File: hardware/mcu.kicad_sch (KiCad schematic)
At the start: 32 parts, among them J301 USB_C_Receptacle_USB2.0, SW301 RESET, SW302 BOOTSEL, U301 USBLC6-2SC6, U302 ESP32-C3, Y301 40 MHz

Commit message: WIP pcb layout
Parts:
- removed L302: CMF3216F-900-2P-T, lzptr:CMC-1206, symbol Device:Filter_EMI_LL_1423
- J301: symbol Connector:USB_C_Receptacle_USB2.0_14P -> Connector:USB_C_Receptacle_USB2.0_16P
- SW302: value BOOTSEL -> BOOT
- renumbered L303 to L302
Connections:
- net USB_CMC_D+ is gone; now on net USB_D+: U301.4 (I/O2)
- net USB_CMC_D- is gone; now on net USB_D-: U301.6 (I/O1)
- net ACT: now also U302.16 (GPIO10); no longer U302.9 (MTMS/GPIO4/ADC1_CH4)
- net I2C_CLK: now also U302.8 (GPIO3/ADC1_CH3); no longer U302.5 (XTAL_32K_N/ADC1_CH1)
- net I2C_DATA: now also U302.9 (MTMS/GPIO4/ADC1_CH4); no longer U302.4 (XTAL_32K_P/ADC1_CH0)
- net LNA_IN: now reaches C304.1, L301.2, U302.1 (LNA_IN)
- net GP8: now reaches R305.2, U302.14 (GPIO8)
- net GP2: now reaches R304.2, U302.6 (GPIO2/ADC1_CH2)
- no-connect marks 14 -> 16
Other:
- note added: "Flash efuses to fixed 3.3V to use MTDI as normal pin https://docs.espressif.com/projects/esptool/en/latest/esp32c3/espefuse/set-flash-voltage-cmd.html"
- note added: "Signal Path: Connector <-> ESD Protection <-> MCU"
- note removed: "Common-Mode Choke Impedance: 90R"
- note removed: "Pull MTDI low or leave unconnected to use internal regulator for the in package Flash Leave VDD_SPI unconnected https://docs.espressif.com/projects/esptool/en/latest/esp32c3/espefuse/set-flash-voltage-cmd.html"
- note removed: "Signal Path: Connector <-> ESD Protection <-> Common-Mode Choke <-> MCU"

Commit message: Finished the pcb layout
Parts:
- AE301: footprint lzptr:ANT_16060A1T_WAL-L -> lzptr:ANT5320LL45R2400A; MPN C127620 -> C723371
- D301: MPN C72043 -> C12624
- J301: Position Offset (none) -> 0,1.45
- U302: value ESP32-C3 -> ESP32-C3FH4; MPN (none) -> C2858491; Rotation Offset (none) -> -90
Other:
- note added: "CL = 10pF"
- note removed: "CL = 9pF"
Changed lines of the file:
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@@
 		)
 	)
-	(text "CL = 9pF"
+	(text "CL = 10pF"
 		(exclude_from_sim no)
 		(at 63.246 75.692 0)
@@
 			)
 		)
-		(property "Value" "ESP32-C3"
+		(property "Value" "ESP32-C3FH4"
 			(at 153.3241 119.38 0)
 			(effects
@@
 			)
 		)
-		(property "MPN" ""
+		(property "MPN" "C2858491"
+			(at 151.13 86.36 0)
+			(effects
+				(font
+					(size 1.27 1.27)
+				)
+				(hide yes)
+			)
+		)
+		(property "Rotation Offset" "-90"
 			(at 151.13 86.36 0)
 			(effects
@@
 			)
 		)
-		(property "Footprint" "lzptr:ANT_16060A1T_WAL-L"
+		(property "Footprint" "lzptr:ANT5320LL45R2400A"
 			(at 58.42 49.53 0)
 			(effects
@@
 			)
 		)
-		(property "MPN" "C127620"
+		(property "MPN" "C723371"
 			(at 58.42 49.53 0)
 			(effects
@@
 			)
 		)
-		(property "MPN" "C72043"
+		(property "MPN" "C12624"
 			(at 267.97 135.89 0)
 			(effects
@@
 			)
 		)
+		(property "Position Offset" "0,1.45"
+			(at 43.18 162.56 0)
+			(effects
+				(font
+					(size 1.27 1.27)
+				)
+				(hide yes)
+			)
+		)

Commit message: release: v0.1
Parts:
- AE301: footprint lzptr:ANT5320LL45R2400A -> lzptr:Rainsun-AN9520-245; MPN C723371 -> C99665
- D301: footprint LED_SMD:LED_0603_1608Metric -> LED_SMD:LED_0805_2012Metric; MPN C12624 -> C2297
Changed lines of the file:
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@@
 	(title_block
 		(title "Radiator Booster")
-		(date "2024-11-17")
+		(date "2025-01-19")
 		(rev "0.1")
 		(company "LP")
@@
 			)
 		)
-		(property "Footprint" "lzptr:ANT5320LL45R2400A"
+		(property "Footprint" "lzptr:Rainsun-AN9520-245"
 			(at 58.42 49.53 0)
 			(effects
@@
 			)
 		)
-		(property "MPN" "C723371"
+		(property "MPN" "C99665"
 			(at 58.42 49.53 0)
 			(effects
@@
 			)
 		)
-		(property "Footprint" "LED_SMD:LED_0603_1608Metric"
+		(property "Footprint" "LED_SMD:LED_0805_2012Metric"
 			(at 267.97 135.89 0)
 			(effects
@@
 			)
 		)
-		(property "MPN" "C12624"
+		(property "MPN" "C2297"
 			(at 267.97 135.89 0)
 			(effects

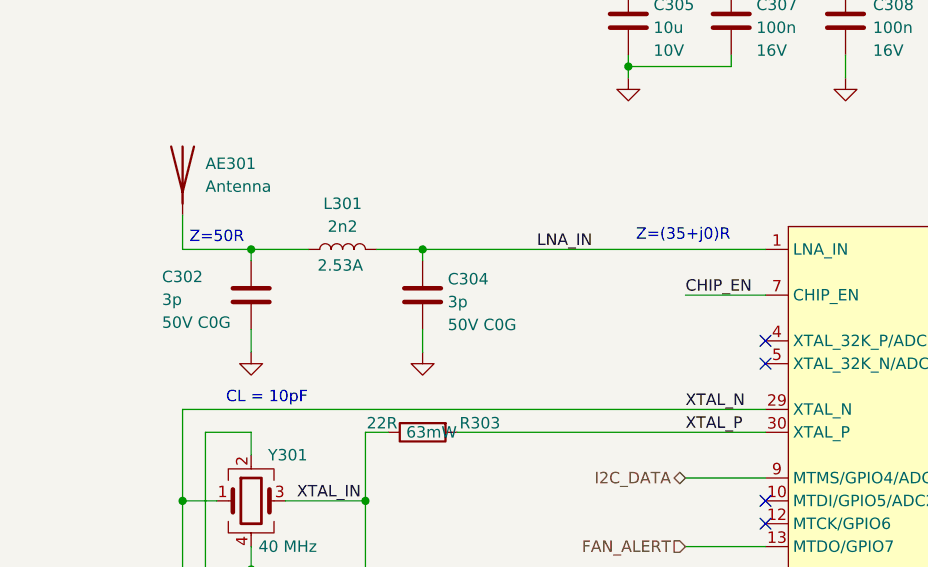
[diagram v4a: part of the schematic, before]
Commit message: Fixed routing at intel pwm fan connectors
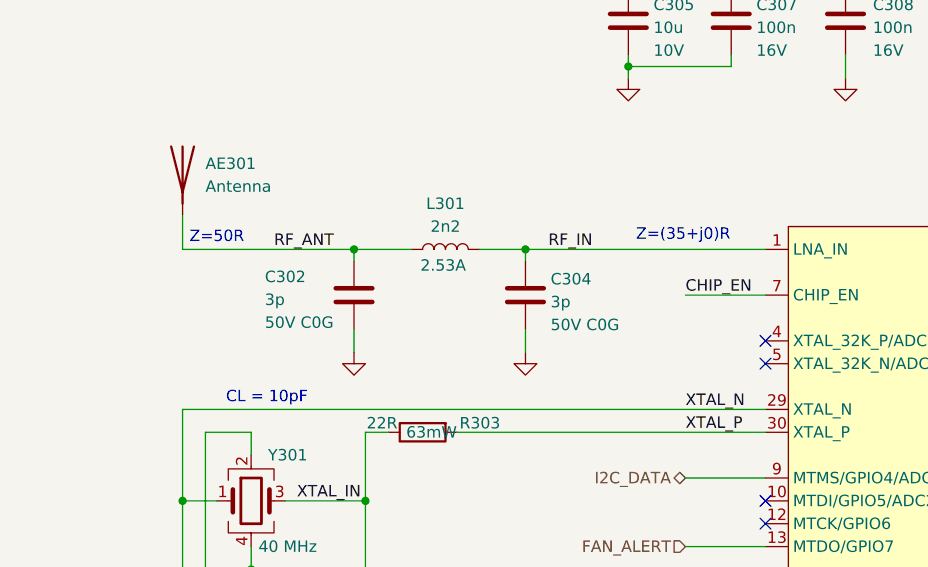
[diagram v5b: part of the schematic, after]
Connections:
- net RF_ANT: now reaches AE301.1 (A), C302.1, L301.1
- net LNA_IN renamed RF_IN
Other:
- moved on the sheet: C302, C304, L301
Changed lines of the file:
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@@
 	)
 	(junction
-		(at 85.09 58.42)
+		(at 96.52 58.42)
 		(diameter 0)
 		(color 0 0 0 0)
@@
 	)
 	(junction
-		(at 66.04 58.42)
+		(at 77.47 58.42)
 		(diameter 0)
 		(color 0 0 0 0)
@@
 	(wire
 		(pts
-			(xy 72.39 58.42) (xy 66.04 58.42)
+			(xy 83.82 58.42) (xy 77.47 58.42)
 		)
 		(stroke
@@
 	(wire
 		(pts
-			(xy 85.09 67.31) (xy 85.09 69.85)
+			(xy 96.52 67.31) (xy 96.52 69.85)
 		)
 		(stroke
@@
 	(wire
 		(pts
-			(xy 85.09 58.42) (xy 85.09 59.69)
+			(xy 96.52 58.42) (xy 96.52 59.69)
 		)
 		(stroke
@@
 	(wire
 		(pts
-			(xy 66.04 58.42) (xy 66.04 59.69)
+			(xy 77.47 58.42) (xy 77.47 59.69)
 		)
 		(stroke
@@
 	(wire
 		(pts
-			(xy 123.19 58.42) (xy 85.09 58.42)
-		)
-		(stroke
-			(width 0)
-			(type default)
-		)
-	)
-	(wire
-		(pts
 			(xy 78.74 160.02) (xy 63.5 160.02)
 		)
@@
 	(wire
 		(pts
-			(xy 80.01 58.42) (xy 85.09 58.42)
+			(xy 91.44 58.42) (xy 96.52 58.42)
 		)
 		(stroke
@@
 	(wire
 		(pts
-			(xy 58.42 58.42) (xy 66.04 58.42)
+			(xy 58.42 58.42) (xy 77.47 58.42)
 		)
 		(stroke
@@
 	(wire
 		(pts
+			(xy 96.52 58.42) (xy 123.19 58.42)
+		)
+		(stroke
+			(width 0)
+			(type default)
+		)
+	)
+	(wire
+		(pts
 			(xy 153.67 41.91) (xy 156.21 41.91)
 		)
@@
 	(wire
 		(pts
-			(xy 66.04 69.85) (xy 66.04 67.31)
+			(xy 77.47 69.85) (xy 77.47 67.31)
 		)
 		(stroke
@@
 		)
 	)
+	(label "RF_ANT"
+		(at 68.58 58.42 0)
+		(effects
+			(font
+				(size 1.27 1.27)
+			)
+			(justify left bottom)
+		)
+	)
 	(label "XTAL_N"
 		(at 114.3 76.2 0)
@@
 		)
 	)
-	(label "LNA_IN"
-		(at 97.79 58.42 0)
+	(label "RF_IN"
+		(at 99.06 58.42 0)
 		(effects
 			(font
@@
 	(symbol
 		(lib_id "power:GND")
-		(at 66.04 69.85 0)
+		(at 77.47 69.85 0)
 		(unit 1)
 		(exclude_from_sim no)
@@
 		(fields_autoplaced yes)
 		(property "Reference" "#PWR0303"
-			(at 66.04 76.2 0)
+			(at 77.47 76.2 0)
 			(effects
 				(font
@@
 		)
 		(property "Value" "GND"
-			(at 66.04 74.93 0)
+			(at 77.47 74.93 0)
 			(effects
 				(font
@@
 		)
 		(property "Footprint" ""
-			(at 66.04 69.85 0)
+			(at 77.47 69.85 0)
 			(effects
 				(font
@@
 		)
 		(property "Datasheet" ""
-			(at 66.04 69.85 0)
+			(at 77.47 69.85 0)
 			(effects
 				(font
@@
 		)
 		(property "Description" "Power symbol creates a global label with name \"GND\" , ground"
-			(at 66.04 69.85 0)
+			(at 77.47 69.85 0)
 			(effects
 				(font
@@
 		)
 		(property "Rating" ""
-			(at 66.04 69.85 0)
+			(at 77.47 69.85 0)
 			(effects
 				(font
@@
 		)
 		(property "MPN" ""
-			(at 66.04 69.85 0)
+			(at 77.47 69.85 0)
 			(effects
 				(font
@@
 	(symbol
 		(lib_id "Device:C")
-		(at 85.09 63.5 0)
+		(at 96.52 63.5 0)
 		(unit 1)
 		(exclude_from_sim no)
@@
 		(dnp no)
 		(property "Reference" "C304"
-			(at 87.884 61.722 0)
+			(at 99.314 61.722 0)
 			(effects
 				(font
@@
 		)
 		(property "Value" "3p"
-			(at 87.884 64.262 0)
+			(at 99.314 64.262 0)
 			(effects
 				(font
@@
 		)
 		(property "Footprint" "Capacitor_SMD:C_0402_1005Metric"
-			(at 86.0552 67.31 0)
+			(at 97.4852 67.31 0)
 			(effects
 				(font
@@
 		)
 		(property "Datasheet" "~"
-			(at 85.09 63.5 0)
+			(at 96.52 63.5 0)
 			(effects
 				(font
@@
 		)
 		(property "Description" "Unpolarized capacitor"
-			(at 85.09 63.5 0)
+			(at 96.52 63.5 0)
 			(effects
 				(font
@@
 		)
 		(property "MPN" "C1564"
-			(at 85.09 63.5 0)
+			(at 96.52 63.5 0)
 			(effects
 				(font
@@
 		)
 		(property "Rating" "50V C0G"
-			(at 87.884 66.802 0)
+			(at 99.314 66.802 0)
 			(effects
 				(font
@@
 	(symbol
 		(lib_id "Device:L")
-		(at 76.2 58.42 90)
+		(at 87.63 58.42 90)
 		(unit 1)
 		(exclude_from_sim no)
@@
 		(dnp no)
 		(property "Reference" "L301"
-			(at 76.2 53.34 90)
+			(at 87.63 53.34 90)
 			(effects
 				(font
@@
 		)
 		(property "Value" "2n2"
-			(at 76.2 55.88 90)
+			(at 87.63 55.88 90)
 			(effects
 				(font
@@
 		)
 		(property "Footprint" "Inductor_SMD:L_0402_1005Metric"
-			(at 76.2 58.42 0)
+			(at 87.63 58.42 0)
 			(effects
 				(font
@@
 		)
 		(property "Datasheet" "~"
-			(at 76.2 58.42 0)
+			(at 87.63 58.42 0)
 			(effects
 				(font
@@
 		)
 		(property "Description" "Inductor"
-			(at 76.2 58.42 0)
+			(at 87.63 58.42 0)
 			(effects
 				(font
@@
 		)
 		(property "Rating" "2.53A"
-			(at 75.946 60.198 90)
+			(at 87.376 60.198 90)
 			(effects
 				(font
@@
 		)
 		(property "MPN" "C412264"
-			(at 76.2 58.42 0)
+			(at 87.63 58.42 0)
 			(effects
 				(font
@@
 	(symbol
 		(lib_id "Device:C")
-		(at 66.04 63.5 0)
+		(at 77.47 63.5 0)
 		(unit 1)
 		(exclude_from_sim no)
@@
 		(dnp no)
 		(property "Reference" "C302"
-			(at 56.134 61.468 0)
+			(at 67.564 61.468 0)
 			(effects
 				(font
@@
 		)
 		(property "Value" "3p"
-			(at 56.134 64.008 0)
+			(at 67.564 64.008 0)
 			(effects
 				(font
@@
 		)
 		(property "Footprint" "Capacitor_SMD:C_0402_1005Metric"
-			(at 67.0052 67.31 0)
+			(at 78.4352 67.31 0)
 			(effects
 				(font
@@
 		)
 		(property "Datasheet" "~"
-			(at 66.04 63.5 0)
+			(at 77.47 63.5 0)
 			(effects
 				(font
@@
 		)
 		(property "Description" "Unpolarized capacitor"
-			(at 66.04 63.5 0)
+			(at 77.47 63.5 0)
 			(effects
 				(font
@@
 		)
 		(property "MPN" "C1564"
-			(at 66.04 63.5 0)
+			(at 77.47 63.5 0)
 			(effects
 				(font
@@
 		)
 		(property "Rating" "50V C0G"
-			(at 56.134 66.548 0)
+			(at 67.564 66.548 0)
 			(effects
 				(font
@@
 	(symbol
 		(lib_id "power:GND")
-		(at 85.09 69.85 0)
+		(at 96.52 69.85 0)
 		(unit 1)
 		(exclude_from_sim no)
@@
 		(fields_autoplaced yes)
 		(property "Reference" "#PWR0305"
-			(at 85.09 76.2 0)
+			(at 96.52 76.2 0)
 			(effects
 				(font
@@
 		)
 		(property "Value" "GND"
-			(at 85.09 74.93 0)
+			(at 96.52 74.93 0)
 			(effects
 				(font
@@
 		)
 		(property "Footprint" ""
-			(at 85.09 69.85 0)
+			(at 96.52 69.85 0)
 			(effects
 				(font
@@
 		)
 		(property "Datasheet" ""
-			(at 85.09 69.85 0)
+			(at 96.52 69.85 0)
 			(effects
 				(font
@@
 		)
 		(property "Description" "Power symbol creates a global label with name \"GND\" , ground"
-			(at 85.09 69.85 0)
+			(at 96.52 69.85 0)
 			(effects
 				(font
@@
 		)
 		(property "Rating" ""
-			(at 85.09 69.85 0)
+			(at 96.52 69.85 0)
 			(effects
 				(font
@@
 		)
 		(property "MPN" ""
-			(at 85.09 69.85 0)
+			(at 96.52 69.85 0)
 			(effects
 				(font

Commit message: Finished layout for rev 0.2
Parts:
- AE301: value Antenna -> ANT3216LL00R2400A; footprint lzptr:Rainsun-AN9520-245 -> lzptr:ANT3216LL00R2400A; MPN C99665 -> C293767
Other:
- note added: "Place 10u close to Pin17"
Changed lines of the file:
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@@
 		)
 	)
+	(text "Place 10u close to Pin17\n"
+		(exclude_from_sim no)
+		(at 205.74 30.48 0)
+		(effects
+			(font
+				(size 1.27 1.27)
+			)
+			(justify left bottom)
+		)
+	)
 	(junction
 		(at 153.67 41.91)
@@
 			)
 		)
-		(property "Value" "Antenna"
+		(property "Value" "ANT3216LL00R2400A"
 			(at 60.96 51.4349 0)
 			(effects
@@
 			)
 		)
-		(property "Footprint" "lzptr:Rainsun-AN9520-245"
+		(property "Footprint" "lzptr:ANT3216LL00R2400A"
 			(at 58.42 49.53 0)
 			(effects
@@
 			)
 		)
-		(property "MPN" "C99665"
+		(property "MPN" "C293767"
 			(at 58.42 49.53 0)
 			(effects
@@
 			(at 267.97 135.89 0)
 			(effects
+				(font
+					(size 1.27 1.27)
+				)
+				(hide yes)
+			)
+		)
+		(property "Sim.Pins" "1=K 2=A"
+			(at 267.97 135.89 0)
+			(effects

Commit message: Updated matching network. Changed inductor for all filter for bom sonsolidation after matching network changes
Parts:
- C302, C304: MPN C1564 -> C88891
- L301, L302: value 2n2 -> 2n3; MPN C412264 -> C412340; Rating 2.53A -> 1A
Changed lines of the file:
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@@
 			)
 		)
-		(property "MPN" "C1564"
+		(property "MPN" "C88891"
 			(at 96.52 63.5 0)
 			(effects
@@
 			)
 		)
-		(property "Value" "2n2"
+		(property "Value" "2n3"
 			(at 87.63 55.88 90)
 			(effects
@@
 			)
 		)
-		(property "Rating" "2.53A"
+		(property "Rating" "1A"
 			(at 87.376 60.198 90)
 			(effects
@@
 			)
 		)
-		(property "MPN" "C412264"
+		(property "MPN" "C412340"
 			(at 87.63 58.42 0)
 			(effects
@@
 			)
 		)
-		(property "MPN" "C1564"
+		(property "MPN" "C88891"
 			(at 77.47 63.5 0)
 			(effects
@@
 			)
 		)
-		(property "Value" "2n2"
+		(property "Value" "2n3"
 			(at 125.73 24.13 90)
 			(effects
@@
 			)
 		)
-		(property "Rating" "2.53A"
+		(property "Rating" "1A"
 			(at 125.73 27.686 90)
 			(effects
@@
 			)
 		)
-		(property "MPN" "C412264"
+		(property "MPN" "C412340"
 			(at 125.73 26.67 0)
 			(effects
